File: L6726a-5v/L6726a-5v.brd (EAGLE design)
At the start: 100 x 19 mm, 32 parts, among them IC1 L6727A, U1 5V

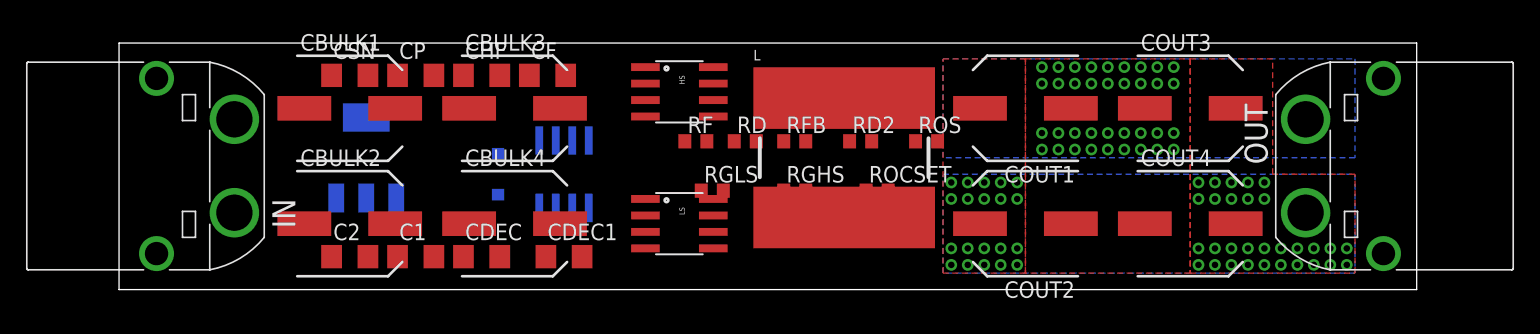
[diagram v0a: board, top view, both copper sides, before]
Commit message: renamed files and folders, layout mostly complete
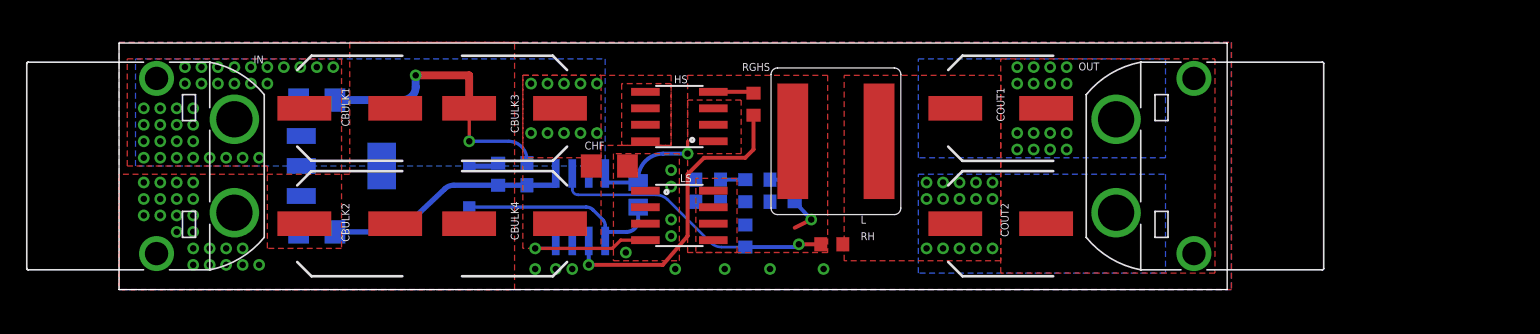
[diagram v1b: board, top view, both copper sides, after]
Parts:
- removed C1, C2, CDEC1: (no value), rcl:C1206
- removed COUT3, COUT4: (no value), rcl:SANYO-OSCON_SMD_E7
- removed D1: (no value), SparkFun-DiscreteSemi:SOD-123
- removed RD2, RF, RFB, RGLS, ROCSET, ROS: (no value), rcl:R0603
- added CBOOT: 100n, rcl:C0805
- added CVRIN, CVROUT: (no value), rcl:C1206
- added D: BAT54, SparkFun-DiscreteSemi:SOD-123
- added RC: 4K7, rcl:R0603
- added RH: 4K640, rcl:R0603
- added RL: 887R, rcl:R0603
- added RSN: 2R2, rcl:R0603
- CBULK1, CBULK2, CBULK3, CBULK4: value (none) -> 33u
- CDEC: value (none) -> 1u; device rcl:C1206 -> rcl:C0603
- CF: value (none) -> 33n; device rcl:C1206 -> rcl:C0603
- CHF: value (none) -> 10u
- COUT1, COUT2: value (none) -> 220u
- CP: value (none) -> 150p; device rcl:C1206 -> rcl:C0603
- CSN: value (none) -> 3.3n; device rcl:C1206 -> rcl:C0603
- IN: value XT60PW-M -> IN
- L: device SparkFun-Passives:INDUCTOR_SDR1307 -> coilcraft:XAL1010
- OUT: value XT60PW-M -> OUT
- RD, RGHS: value (none) -> 2R2
- moved CSN 33.6 mm to (50.2, 7.62), flipped to the bottom, turned to 270 degrees
- moved CP 23.3 mm to (44.5, 7.62), flipped to the bottom, turned to 90 degrees
- moved RD 19.2 mm to (29.2, 8.89), flipped to the bottom, turned to 90 degrees
- moved CF 16.0 mm to (46.4, 7.62), flipped to the bottom, turned to 90 degrees
- moved OUT 14.6 mm to (76.8, 9.53)
- moved CHF 12.1 mm to (37.8, 9.53)
- moved RGHS 7.38 mm to (48.9, 14.3), turned to 90 degrees
- moved CDEC 7.25 mm to (31.4, 8.89), flipped to the bottom, turned to 90 degrees
- moved IC1 2.84 mm to (35.6, 6.35)
- moved U1 2.01 mm to (17.1, 9.53), turned to 90 degrees
- moved COUT1 1.91 mm to (67.9, 14.0)
- moved COUT2 1.91 mm to (67.9, 5.08)
- moved HS 1.90 mm to (43.2, 13.3), turned to 90 degrees
- moved L 1.42 mm to (55.2, 11.4)
- moved LS 0.63 mm to (43.2, 5.71)
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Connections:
- removed net LGATE`: IC1.4, RGLS.1, ROCSET.1
- removed net N$2: CDEC1.1, IC1.1, RD.2
- new net BOOT: CBOOT.1, D.C, IC1.1
- net +12V: now also CVRIN.1; no longer C2.1
- net FB: now also RH.1, RL.1; no longer RFB.1, ROS.1
- net GND: now also CVRIN.2, CVROUT.2, RC.2, RL.2; no longer C1.2, C2.2, COUT3.-, COUT4.-, RF.2, ROCSET.2, ROS.2
- net LGATE: now also IC1.4; no longer RGLS.2
- net N$1: now also D.A, RD.2; no longer D1.C, RD.1
- net N$3: now also RC.1; no longer RF.1
- net PHASE: now also CBOOT.2, RSN.1; no longer CDEC1.2, RD2.1
- net RSN: now also RSN.2; no longer RD2.2
- net VCC: now also CVROUT.1, RD.1; no longer C1.1, D1.A
- net VOUT: now also RH.2; no longer COUT3.+, COUT4.+, RFB.2
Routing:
- net UGATE`: track 0.00 -> 23.8 mm, vias 0 -> 1
- net FB: track 0.00 -> 22.1 mm, vias 0 -> 1
- net GND: track 0.00 -> 22.0 mm, vias 36 -> 53
- net VCC: track 0.00 -> 19.2 mm
- net BOOT: track 0.00 -> 16.2 mm
- net PHASE: track 0.00 -> 12.4 mm, vias 0 -> 2
- net LGATE: track 0.00 -> 10.9 mm, vias 0 -> 1
- net UGATE: track 0.00 -> 3.20 mm
- net N$1: track 0.00 -> 2.45 mm
- net RSN: track 0.00 -> 1.91 mm
- net N$3: track 0.00 -> 1.91 mm
- added copper zone on layer 1, net +12V
- added copper zone on layer 16, net +12V
- added copper zone on layer 1, net PHASE
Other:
- board size 100 x 19 mm -> 85.4 x 19 mm

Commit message: lots of progress with routing, verifying component packages
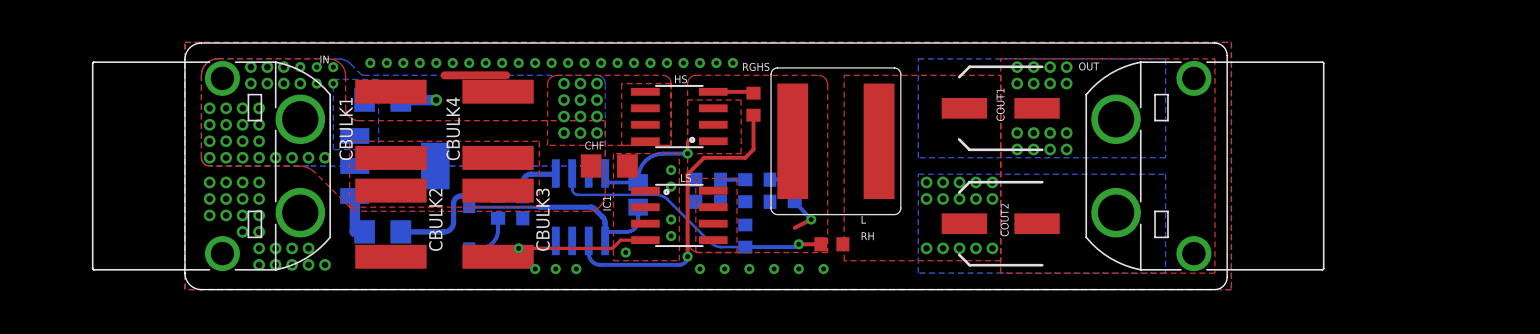
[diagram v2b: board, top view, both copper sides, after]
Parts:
- CBULK1, CBULK2, CBULK3, CBULK4: device rcl:SANYO-OSCON_SMD_E7 -> rcl:C2220K
- COUT1, COUT2: value 220u -> 330u; device rcl:SANYO-OSCON_SMD_E7 -> rcl:SANYO-OSCON_SMD_C6
- moved CBULK3 8.98 mm to (29.2, 5.08), turned to 270 degrees
- moved CBULK4 7.73 mm to (29.2, 12.7), turned to 90 degrees
- moved CVRIN 5.08 mm to (20.3, 14.6)
- moved CVROUT 5.08 mm to (20.3, 4.45)
- moved IN 5.08 mm to (14.0, 9.53)
- moved U1 4.13 mm to (21.3, 9.53)
- moved CBULK1 3.42 mm to (21.0, 12.7), turned to 90 degrees
- moved D 3.17 mm to (27.0, 4.76), turned to 270 degrees
- moved CBULK2 3.17 mm to (21.0, 5.08), turned to 270 degrees
- moved CDEC 2.56 mm to (31.1, 6.35), turned to 270 degrees
- moved RD 2.54 mm to (29.2, 6.35), turned to 270 degrees
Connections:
- net +12V: now also CBULK1.1, CBULK2.1, CBULK3.1, CBULK4.1; no longer CBULK1.+, CBULK2.+, CBULK3.+, CBULK4.+
- net GND: now also CBULK1.2, CBULK2.2, CBULK3.2, CBULK4.2; no longer CBULK1.-, CBULK2.-, CBULK3.-, CBULK4.-
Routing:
- net GND: track 22.0 -> 11.0 mm, vias 53 -> 77
- net VCC: track 19.2 -> 16.2 mm
- net LGATE: track 10.9 -> 13.5 mm
- net N$1: track 2.45 -> 3.73 mm
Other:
- board size 85.4 x 19 mm -> 80.3 x 19 mm

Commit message: changed mosfet package, blew up layout
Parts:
- CF: value 33n -> 15n
- CP: value 150p -> 22p
- HS, LS: device SparkFun-DiscreteSemi:SO08 -> power-mosfet:POWERSO8
- RC: value 4K7 -> 18K0
- RH, RL: device rcl:R0603 -> rcl:R0805
- moved HS 0.71 mm to (43.8, 13.7), turned to 180 degrees
- moved LS 0.63 mm to (43.8, 5.71), turned to 0 degrees
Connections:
- net N$3 renamed CC
- net +12V: now also HS.PAD
- net PHASE: now also LS.PAD
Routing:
- net UGATE`: track 24.1 -> 9.20 mm
- net UGATE: track 3.20 -> 0.10 mm
- net PHASE: track 12.4 -> 13.7 mm
- net GND: vias 77 -> 74

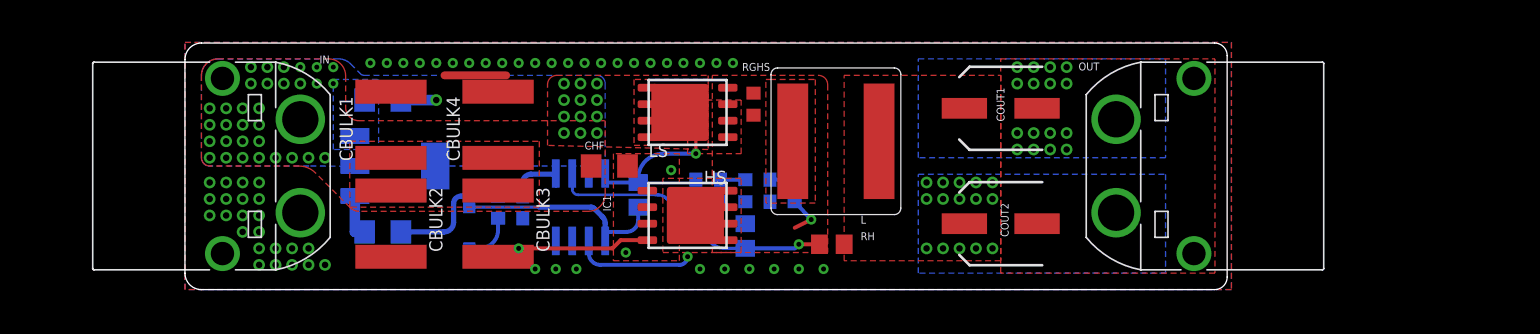
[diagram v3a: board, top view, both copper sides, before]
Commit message: finished routing transistors, still need LDO
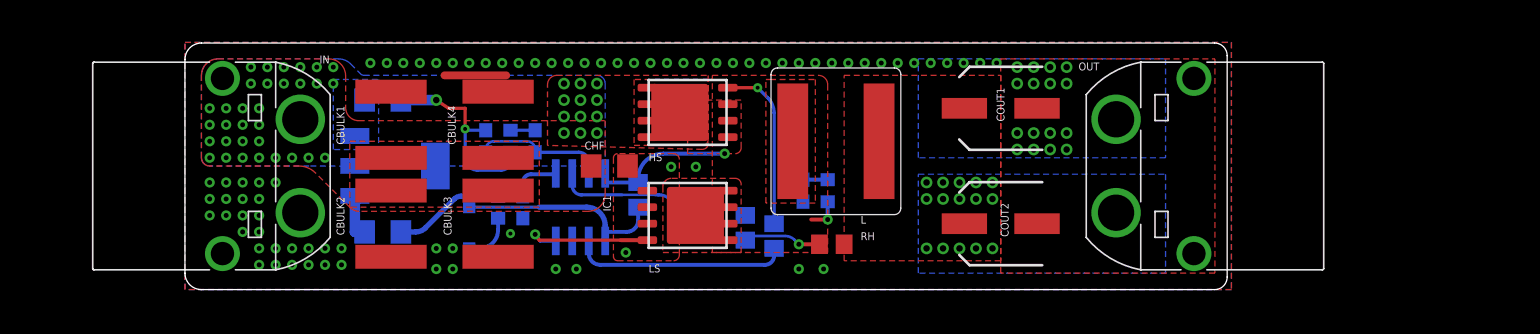
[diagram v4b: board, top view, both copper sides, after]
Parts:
- removed CF: 15n, rcl:C0603
- added CC: 15n, rcl:C0603
- RGHS: device rcl:R0603 -> rcl:R0805
- moved RC 18.5 mm to (30.2, 11.4)
- moved CP 16.6 mm to (28.3, 11.4)
- moved RGHS 10.3 mm to (50.5, 4.13), flipped to the bottom
- moved CSN 2.54 mm to (52.7, 7.62)
- moved RSN 2.54 mm to (54.6, 7.62)
- moved RL 0.63 mm to (48.3, 4.76)
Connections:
- net CC: now also CC.2; no longer CF.2
- net COMP: now also CC.1, IC1.7; no longer CF.1
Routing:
- net UGATE: track 0.10 -> 13.2 mm, vias 0 -> 1
- net GND: track 11.0 -> 23.8 mm, vias 74 -> 96
- net COMP: track 0.00 -> 10.1 mm
- net UGATE`: track 9.20 -> 16.5 mm, vias 1 -> 0
- net LGATE: track 13.6 -> 11.3 mm
- net VCC: track 16.2 -> 15.2 mm

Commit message: a few more tweaks
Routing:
- net GND: track 23.8 -> 19.1 mm

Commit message: finalized layout, I think I'm happy
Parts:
- removed U1: 5V, SparkFun-PowerIC:SOT223
- added IC2: MCP1804, microchip-vreg:SOT23-5
- CVRIN, CVROUT: value (none) -> 1u; device rcl:C1206 -> rcl:C0603
- LS: device power-mosfet:POWERSO8 -> SparkFun-DiscreteSemi:SO08
- moved CVRIN 6.75 mm to (24.8, 9.53), turned to 270 degrees
- moved CVROUT 5.68 mm to (17.8, 9.53), turned to 270 degrees
- moved LS 0.32 mm to (43.5, 5.71), turned to 270 degrees
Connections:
- net +12V: now also IC2.1, IC2.4; no longer U1.3
- net GND: now also IC2.2; no longer U1.1
- net PHASE: no longer LS.PAD
- net VCC: now also IC2.5; no longer U1.2
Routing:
- net VCC: track 15.2 -> 21.8 mm
- net GND: track 19.1 -> 13.5 mm, vias 96 -> 146
- net +12V: track 0.00 -> 2.31 mm

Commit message: finishing touches
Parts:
- IC1: value L6727A -> L6726A; device stm-l6727a:SO-08 -> stm-l6726a:SO-08
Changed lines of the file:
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@@
 <attribute name="NAME" x="25.9715" y="5.6515" size="0.6096" layer="26" font="vector" ratio="14" rot="MR270"/>
 </element>
-<element name="IC1" library="stm-l6727a" package="SO-08" value="L6727A" x="35.56" y="6.35" smashed="yes" rot="MR0">
+<element name="IC1" library="stm-l6726a" package="SO-08" value="L6726A" x="35.56" y="6.35" smashed="yes" rot="MR0">
 <attribute name="NAME" x="33.147" y="6.0325" size="0.6096" layer="25" font="vector" ratio="14" rot="R90"/>
 </element>

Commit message: let the ground pour through between inductor
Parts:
- XT60-IN: value IN -> (none)
- moved RH 4.14 mm to (59.1, 3.81)
- moved CSN 0.63 mm to (52.1, 7.62)
- moved RSN 0.63 mm to (54.0, 7.62)
- renumbered IN to XT60-IN, OUT to XT60-OUT
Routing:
- net FB: track 21.8 -> 25.9 mm
- net PHASE: track 13.6 -> 14.3 mm
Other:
- board text added: "(C) GLM AUGUST 2022"
- board text added: "15-28VDC"
- board text added: "5V"
- board text added: "L6726A BUCK R1"
